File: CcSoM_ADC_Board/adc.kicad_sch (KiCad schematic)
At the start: 17 parts, among them J13 Conn_02x03_Odd_Even, J14 Conn_02x03_Odd_Even, J15 Conn_02x02_Counter_Clockwise, U12 LTC2242IUP-12-PBF

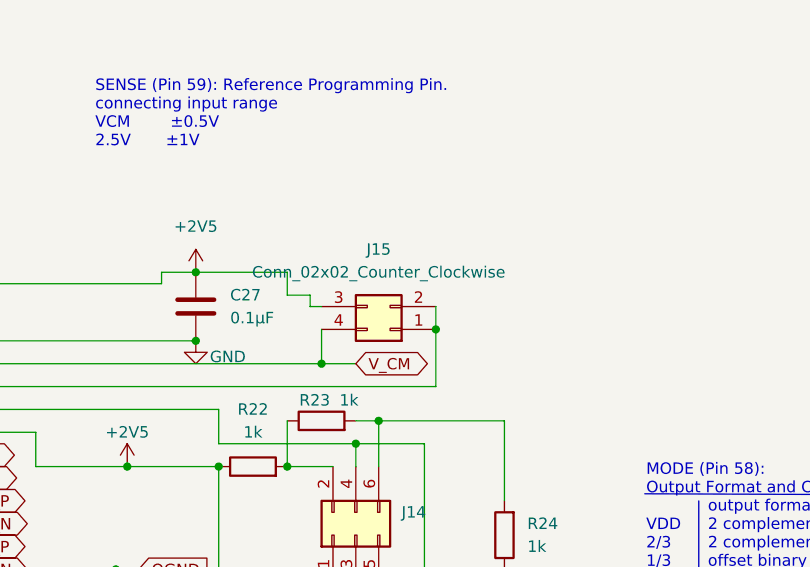
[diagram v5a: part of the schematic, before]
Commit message: changed digikeyno from component, added info into readme about discontinued parts in digikey
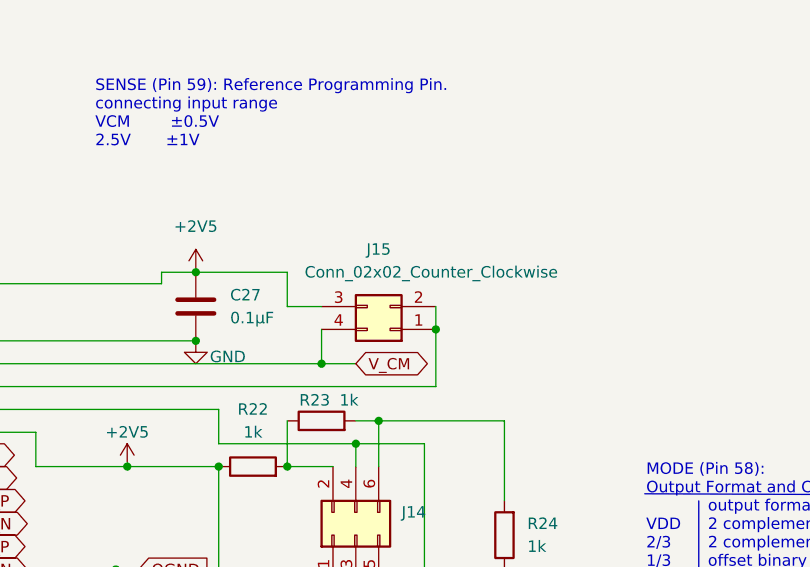
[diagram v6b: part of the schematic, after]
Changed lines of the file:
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@@
 	)
 	(junction
-		(at 123.19 147.32)
+		(at 184.15 142.24)
 		(diameter 0)
 		(color 0 0 0 0)
 	)
 	(junction
-		(at 184.15 142.24)
+		(at 123.19 147.32)
 		(diameter 0)
 		(color 0 0 0 0)
@@
 	(wire
 		(pts
-			(xy 298.45 119.38) (xy 298.45 120.65)
-		)
-		(stroke
-			(width 0)
-			(type default)
-		)
-	)
-	(wire
-		(pts
 			(xy 113.03 160.02) (xy 113.03 151.13)
 		)
@@
 	(wire
 		(pts
-			(xy 295.91 119.38) (xy 298.45 119.38)
+			(xy 295.91 120.65) (xy 299.72 120.65)
 		)
 		(stroke
@@
 	(wire
 		(pts
-			(xy 250.19 132.08) (xy 288.29 132.08)
+			(xy 123.19 147.32) (xy 153.67 147.32)
 		)
 		(stroke
@@
 	(wire
 		(pts
-			(xy 118.11 147.32) (xy 123.19 147.32)
+			(xy 250.19 132.08) (xy 288.29 132.08)
 		)
 		(stroke
@@
 	(wire
 		(pts
-			(xy 298.45 120.65) (xy 299.72 120.65)
-		)
-		(stroke
-			(width 0)
-			(type default)
-		)
-	)
-	(wire
-		(pts
 			(xy 151.13 124.46) (xy 161.29 124.46)
 		)
@@
 	(wire
 		(pts
-			(xy 123.19 147.32) (xy 153.67 147.32)
-		)
-		(stroke
-			(width 0)
-			(type default)
-		)
-	)
-	(wire
-		(pts
 			(xy 250.19 154.94) (xy 273.05 154.94)
 		)
@@
 	(wire
 		(pts
+			(xy 118.11 147.32) (xy 123.19 147.32)
+		)
+		(stroke
+			(width 0)
+			(type default)
+		)
+	)
+	(wire
+		(pts
 			(xy 303.53 138.43) (xy 303.53 135.89)
 		)
@@
 	(wire
 		(pts
-			(xy 295.91 116.84) (xy 295.91 119.38)
+			(xy 295.91 116.84) (xy 295.91 120.65)
 		)
 		(stroke
@@
 		(on_board yes)
 		(dnp no)
-		(fields_autoplaced yes)
 		(property "Reference" "J15"
 			(at 306.07 114.3 0)
@@
 		)
 		(property "Value" "Conn_02x02_Counter_Clockwise"
-			(at 306.07 116.84 0)
+			(at 311.912 116.84 0)
 			(effects
 				(font
